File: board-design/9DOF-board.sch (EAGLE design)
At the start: 0 parts

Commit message: added arduino and connectors
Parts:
- added I2C, VIN: 22-23-2021, con-molex:22-23-2021
- added SERVO1, SERVO2, SERVO3, SERVO4, SERVO5, SERVO6, SERVO7, SERVO8, SERVO9: 22-23-2041, con-molex:22-23-2041
- added U$1, U$2: PRO-MINI, Arduino-clone:PRO-MINI

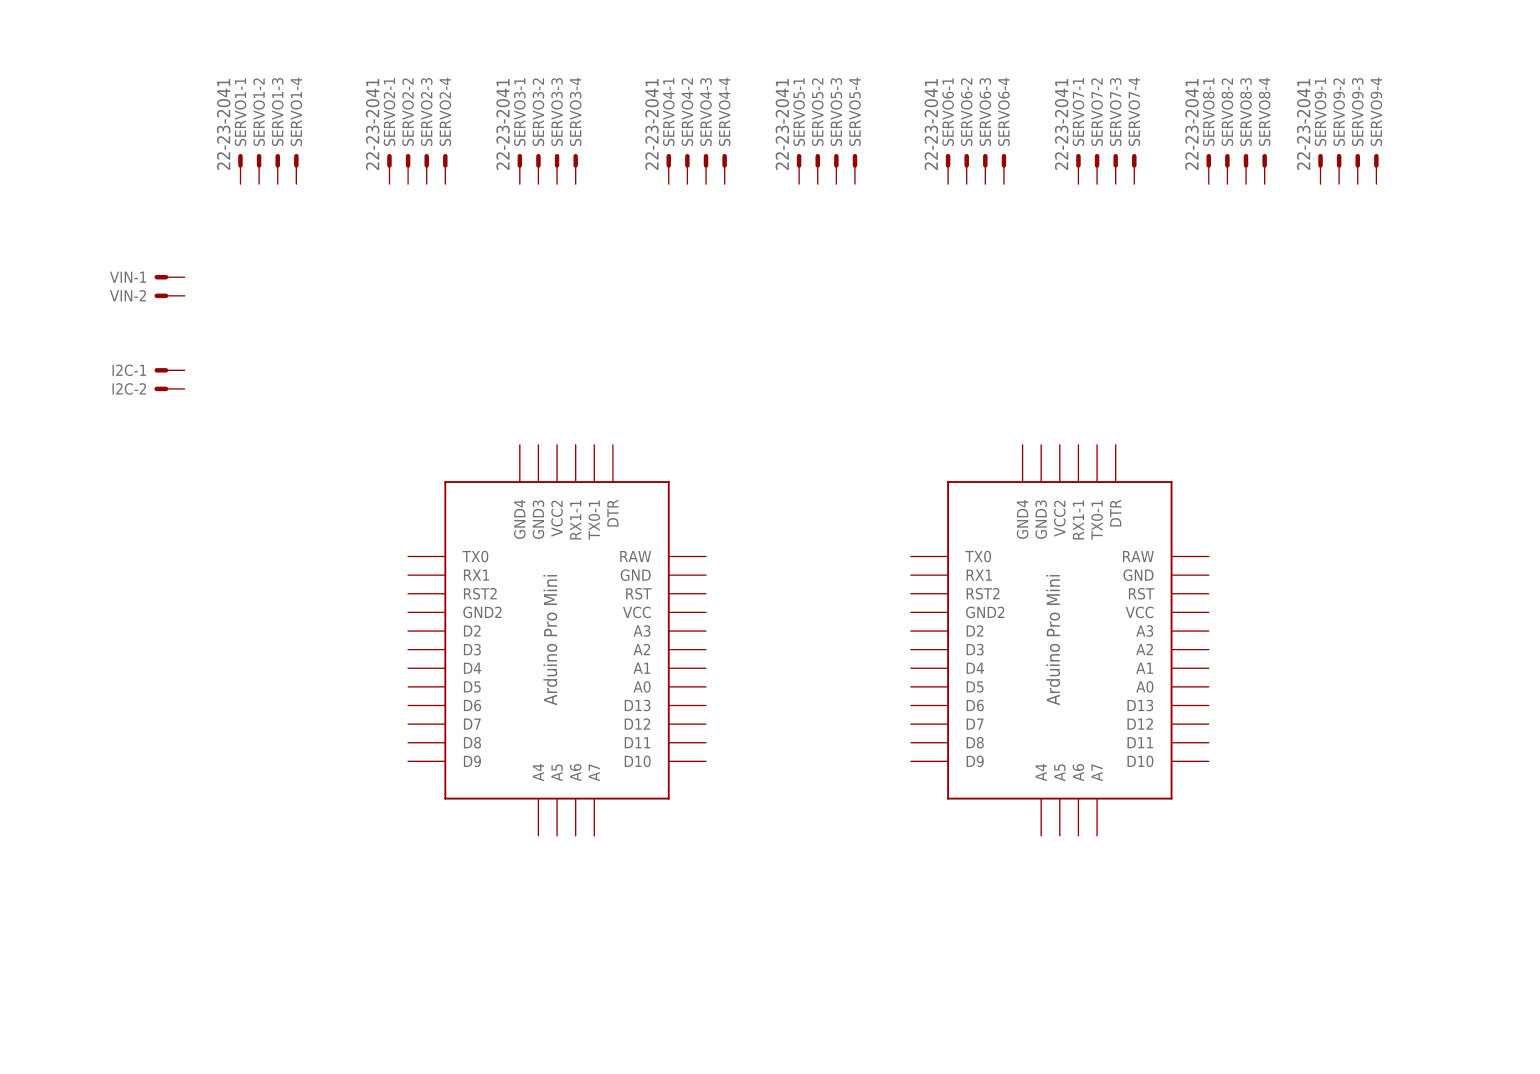
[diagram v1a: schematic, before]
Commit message: First connections between uC and external connectors.
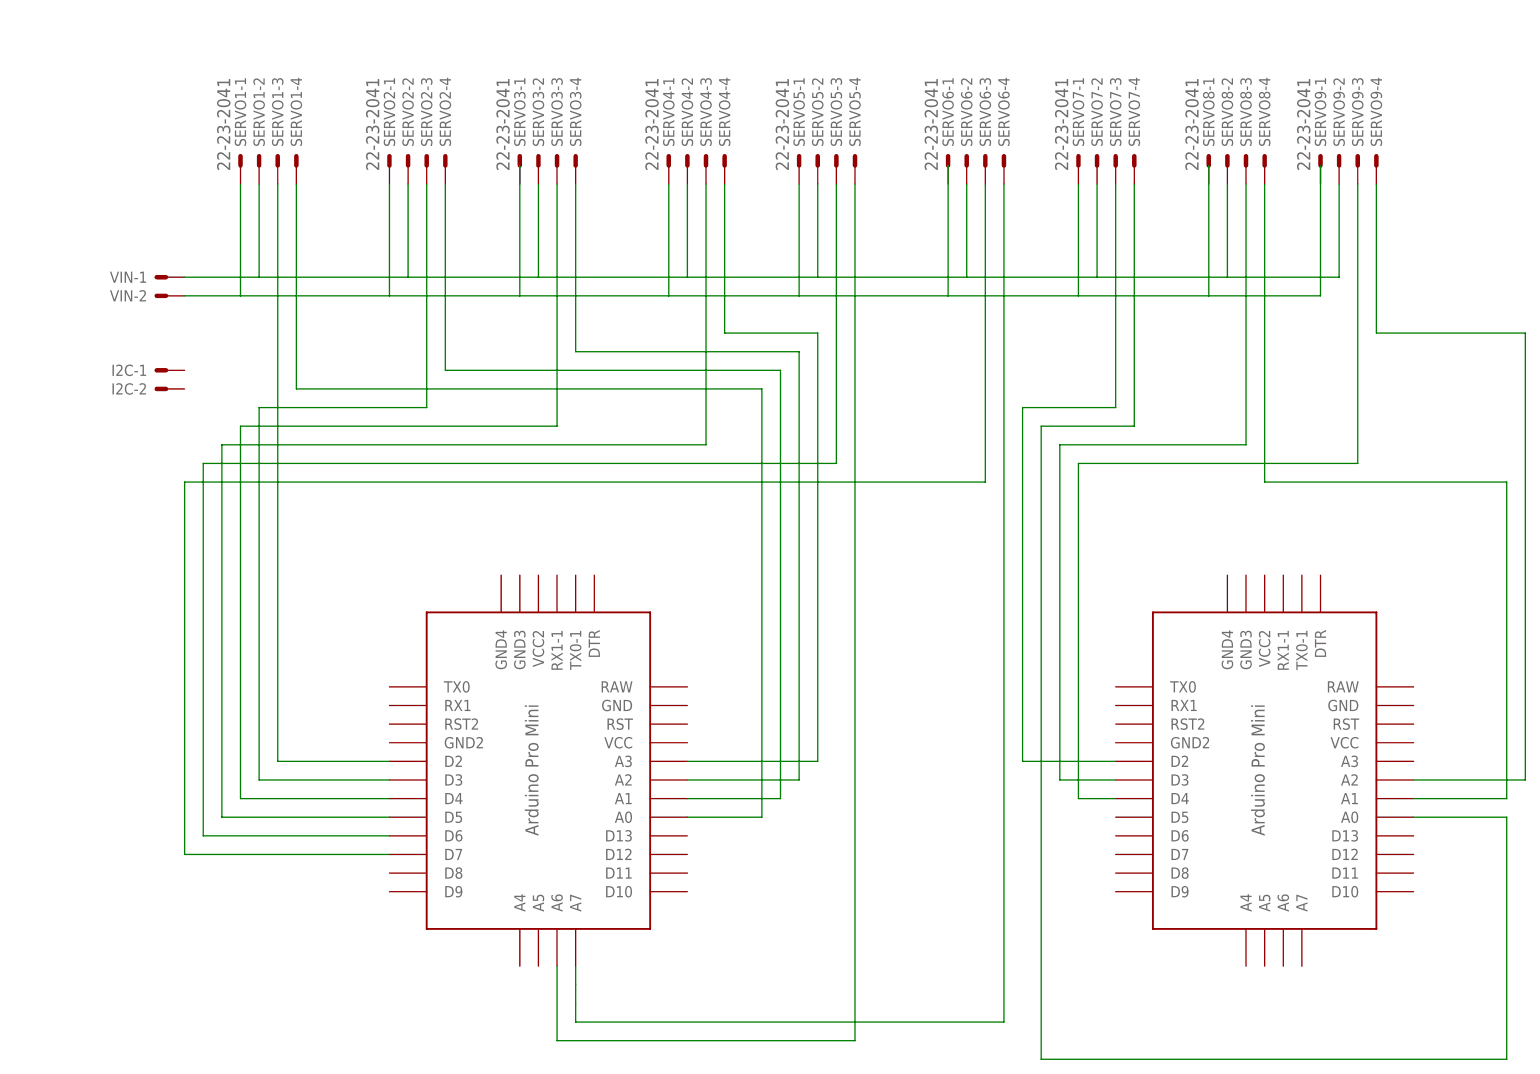
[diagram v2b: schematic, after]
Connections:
- new net N$1: SERVO1-4.S, U$1.A0
- new net N$10: SERVO9-4.S, U$2.A2
- new net N$11: SERVO6-4.S, U$1.A7
- new net N$12: SERVO2-3.S, U$1.D3
- new net N$13: SERVO7-4.S, U$2.A0
- new net N$14: SERVO3-3.S, U$1.D4
- new net N$15: SERVO4-3.S, U$1.D5
- new net N$16: SERVO5-3.S, U$1.D6
- new net N$17: SERVO6-3.S, U$1.D7
- new net N$18: SERVO8-4.S, U$2.A1
- new net N$19: SERVO9-3.S, U$2.D4
- new net N$2: SERVO2-4.S, U$1.A1
- new net N$20: SERVO7-3.S, U$2.D2
- new net N$3: SERVO3-4.S, U$1.A2
- new net N$4: SERVO4-4.S, U$1.A3
- new net N$5: SERVO1-3.S, U$1.D2
- new net N$6: SERVO1-1.S, SERVO2-1.S, SERVO4-1.S, SERVO5-1.S, SERVO7-1.S, VIN-2.S
- new net N$7: SERVO8-3.S, U$2.D3
- new net N$8: SERVO5-4.S, U$1.A6
- new net N$9: SERVO1-2.S, SERVO2-2.S, SERVO3-2.S, SERVO4-2.S, SERVO5-2.S, SERVO6-2.S, SERVO7-2.S, SERVO8-2.S, SERVO9-2.S, VIN-1.S

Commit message: Add files via upload
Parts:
- removed VIN: 22-23-2021, con-molex:22-23-2021
- added J1, VINARDUINO: 22-23-2021, con-molex:22-23-2021
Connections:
- net N$1 renamed SERVO1_POT
- net N$10 renamed SERVO9_POT
- net N$11 renamed SERVO6_POT
- net N$12 renamed SERVO2_SIG
- net N$13 renamed SERVO7_POT
- net N$14 renamed SERVO3_SIG
- net N$15 renamed SERVO4_SIG
- net N$16 renamed SERVO5_SIG
- net N$17 renamed SERVO6_SIG
- net N$18 renamed SERVO8_POT
- net N$19 renamed SERVO9_SIG
- net N$2 renamed SERVO2_POT
- net N$20 renamed SERVO7_SIG
- net N$3 renamed SERVO3_POT
- net N$4 renamed SERVO4_POT
- net N$5 renamed SERVO1_SIG
- net N$7 renamed SERVO8_SIG
- net N$8 renamed SERVO5_POT
- removed net N$6: SERVO1-1.S, SERVO2-1.S, SERVO4-1.S, SERVO5-1.S, SERVO7-1.S, VIN-2.S
- removed net N$9: SERVO1-2.S, SERVO2-2.S, SERVO3-2.S, SERVO4-2.S, SERVO5-2.S, SERVO6-2.S, SERVO7-2.S, SERVO8-2.S, SERVO9-2.S, VIN-1.S
- new net GND: J1-2.S, SERVO1-1.S, SERVO2-1.S, SERVO3-1.S, SERVO4-1.S, SERVO6-1.S, SERVO7-1.S, SERVO8-1.S, SERVO9-1.S, U$1.GND, U$1.GND3, U$1.GND4, U$2.GND, U$2.GND3, U$2.GND4, VINARDUINO-2.S
- new net I2C_SCL: I2C-2.S, U$1.A5
- new net I2C_SDA: I2C-1.S, U$1.A4
- new net VCC_ARDUINO: U$1.VCC2, U$2.VCC2, VINARDUINO-1.S
- new net VCC_SERVO: J1-1.S, SERVO1-2.S, SERVO2-2.S, SERVO3-2.S, SERVO4-2.S, SERVO5-2.S, SERVO6-2.S, SERVO7-2.S, SERVO8-2.S, SERVO9-2.S
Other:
- moved on the sheet: SERVO1-1, SERVO1-2, SERVO1-3, SERVO1-4, SERVO2-1, SERVO2-2, SERVO2-3, SERVO2-4, SERVO3-1, SERVO3-2, SERVO3-3, SERVO3-4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

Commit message: SPI connections between Arduinos done
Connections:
- new net SPI_MISO: U$1.D12, U$2.D12
- new net SPI_MOSI: U$1.D11, U$2.D11
- new net SPI_SCLK: U$1.D13, U$2.D13
- new net SPI_SS: U$1.D10, U$2.D10
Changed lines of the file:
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@@
 <setting verticaltext="up"/>
 </settings>
-<grid distance="0.01" unitdist="inch" unit="inch" style="lines" multiple="1" display="yes" altdistance="0.01" altunitdist="inch" altunit="inch"/>
+<grid distance="0.005" unitdist="inch" unit="inch" style="dots" multiple="1" display="yes" altdistance="0.025" altunitdist="inch" altunit="inch"/>
 <layers>
 <layer number="1" name="Top" color="4" fill="1" visible="no" active="no"/>
@@
 </segment>
 </net>
+<net name="SPI_SS" class="0">
+<segment>
+<pinref part="U$1" gate="G$1" pin="D10"/>
+<wire x1="22.098" y1="-27.686" x2="30.607" y2="-27.686" width="0.1524" layer="91"/>
+<label x="17.907" y="-27.305" size="1.27" layer="95"/>
+</segment>
+<segment>
+<pinref part="U$2" gate="G$1" pin="D10"/>
+<wire x1="121.158" y1="-27.686" x2="128.905" y2="-27.686" width="0.1524" layer="91"/>
+<label x="116.967" y="-27.432" size="1.27" layer="95"/>
+</segment>
+</net>
+<net name="SPI_MOSI" class="0">
+<segment>
+<pinref part="U$1" gate="G$1" pin="D11"/>
+<wire x1="22.098" y1="-25.146" x2="30.48" y2="-25.146" width="0.1524" layer="91"/>
+<label x="17.78" y="-24.765" size="1.27" layer="95"/>
+</segment>
+<segment>
+<pinref part="U$2" gate="G$1" pin="D11"/>
+<wire x1="121.158" y1="-25.146" x2="128.905" y2="-25.146" width="0.1524" layer="91"/>
+<label x="116.713" y="-24.892" size="1.27" layer="95"/>
+</segment>
+</net>
+<net name="SPI_MISO" class="0">
+<segment>
+<pinref part="U$1" gate="G$1" pin="D12"/>
+<wire x1="22.098" y1="-22.606" x2="30.099" y2="-22.606" width="0.1524" layer="91"/>
+<label x="17.653" y="-22.225" size="1.27" layer="95"/>
+</segment>
+<segment>
+<pinref part="U$2" gate="G$1" pin="D12"/>
+<wire x1="121.158" y1="-22.606" x2="128.778" y2="-22.606" width="0.1524" layer="91"/>
+<label x="116.713" y="-22.352" size="1.27" layer="95"/>
+</segment>
+</net>
+<net name="SPI_SCLK" class="0">
+<segment>
+<pinref part="U$2" gate="G$1" pin="D13"/>
+<wire x1="121.158" y1="-20.066" x2="128.651" y2="-20.066" width="0.1524" layer="91"/>
+<label x="116.586" y="-19.812" size="1.27" layer="95"/>
+</segment>
+<segment>
+<pinref part="U$1" gate="G$1" pin="D13"/>
+<wire x1="22.098" y1="-20.066" x2="30.099" y2="-20.066" width="0.1524" layer="91"/>
+<label x="17.653" y="-19.812" size="1.27" layer="95"/>
+</segment>
+</net>
